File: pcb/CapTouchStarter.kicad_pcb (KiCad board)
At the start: 2 copper layers, 73.5 x 64 mm, 44 parts, among them J1 USB_C_Receptacle, J2 62684-50110, Q1 SS8050-G, Q2 SS8050-G, SW1 BOOT, SW2 EN, U1 1965-ESP32-WROOM-32E(8MB)CT-ND, U2 AMS1117-3.3, U3 CP2102N-A01-GQFN28

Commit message: Using 3V3 for display VCC.
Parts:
- C1, C3, C4, C5: value 0.1μF -> 0.1μF/50V
- R11: value 22.1KΩ -> 22K1Ω
- R14: value 47.5KΩ -> 47K5Ω
- R15: value 2K (5%) -> 2KΩ
- R17, R18: value 10K -> 10KΩ
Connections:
- J2 pad 1: VBUS -> +3V3
- R1 pad 2: VBUS -> +3V3
- R2 pad 2: VBUS -> +3V3
- R3 pad 2: VBUS -> +3V3
- R4 pad 2: VBUS -> +3V3
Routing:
- net VBUS: track 207.4 -> 90.4 mm, vias 2 -> 0
- net +3V3: track 246.8 -> 265.3 mm
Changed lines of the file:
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@@
     (thickness 1.6)
     (drawings 11)
-    (tracks 651)
+    (tracks 640)
     (zones 0)
     (modules 44)
@@
       (net 48 "Net-(J2-Pad2)"))
     (pad 1 smd rect (at -2 -11.65) (size 0.3 1.1) (layers F.Cu F.Paste F.Mask)
-      (net 15 VBUS))
+      (net 2 +3V3))
   )
   (module Capacitor_SMD:C_0603_1608Metric (layer F.Cu)
@@
       (effects (font (size 1 1) (thickness 0.15)))
     )
-    (fp_text value 0.1μF (at 5.588 -0.1905) (layer F.Fab)
+    (fp_text value 0.1μF/50V (at 5.588 -0.1905) (layer F.Fab)
       (effects (font (size 1 1) (thickness 0.15)))
     )
@@
       (effects (font (size 1 1) (thickness 0.15)))
     )
-    (fp_text value 0.1μF (at 0 1.43) (layer F.Fab)
+    (fp_text value 0.1μF/50V (at 0 1.43) (layer F.Fab)
       (effects (font (size 1 1) (thickness 0.15)))
     )
@@
       (effects (font (size 1 1) (thickness 0.15)))
     )
-    (fp_text value 0.1μF (at -1.283 2.9845 180) (layer F.Fab)
+    (fp_text value 0.1μF/50V (at -1.283 2.9845 180) (layer F.Fab)
       (effects (font (size 1 1) (thickness 0.15)))
     )
@@
       (effects (font (size 1 1) (thickness 0.15)))
     )
-    (fp_text value 0.1μF (at 0.127 -3.048 180) (layer F.Fab)
+    (fp_text value 0.1μF/50V (at 0.127 -3.048 180) (layer F.Fab)
       (effects (font (size 1 1) (thickness 0.15)))
     )
@@
     )
     (pad 2 smd roundrect (at 0.825 0 180) (size 0.8 0.95) (layers F.Cu F.Paste F.Mask) (roundrect_rratio 0.25)
-      (net 15 VBUS))
+      (net 2 +3V3))
     (pad 1 smd roundrect (at -0.825 0 180) (size 0.8 0.95) (layers F.Cu F.Paste F.Mask) (roundrect_rratio 0.25)
       (net 48 "Net-(J2-Pad2)"))
@@
       (net 47 "Net-(J2-Pad3)"))
     (pad 2 smd roundrect (at 0.825 0 180) (size 0.8 0.95) (layers F.Cu F.Paste F.Mask) (roundrect_rratio 0.25)
-      (net 15 VBUS))
+      (net 2 +3V3))
     (model ${KISYS3DMOD}/Resistor_SMD.3dshapes/R_0603_1608Metric.wrl
       (at (xyz 0 0 0))
@@
     )
     (pad 2 smd roundrect (at 0.825 0 180) (size 0.8 0.95) (layers F.Cu F.Paste F.Mask) (roundrect_rratio 0.25)
-      (net 15 VBUS))
+      (net 2 +3V3))
     (pad 1 smd roundrect (at -0.825 0 180) (size 0.8 0.95) (layers F.Cu F.Paste F.Mask) (roundrect_rratio 0.25)
       (net 46 "Net-(J2-Pad4)"))
@@
       (net 45 "Net-(J2-Pad5)"))
     (pad 2 smd roundrect (at 0.825 0 180) (size 0.8 0.95) (layers F.Cu F.Paste F.Mask) (roundrect_rratio 0.25)
-      (net 15 VBUS))
+      (net 2 +3V3))
     (model ${KISYS3DMOD}/Resistor_SMD.3dshapes/R_0603_1608Metric.wrl
       (at (xyz 0 0 0))
@@
       (effects (font (size 1 1) (thickness 0.15)))
     )
-    (fp_text value 22.1KΩ (at -0.635 2.794) (layer F.Fab)
+    (fp_text value 22K1Ω (at -0.635 2.794) (layer F.Fab)
       (effects (font (size 0.8 0.8) (thickness 0.1)))
     )
@@
       (effects (font (size 1 1) (thickness 0.15)))
     )
-    (fp_text value "2K (5%)" (at 0.127 3.6195 270) (layer F.Fab) hide
+    (fp_text value 2KΩ (at 0.127 3.6195 270) (layer F.Fab) hide
       (effects (font (size 0.5 0.5) (thickness 0.1)))
     )
@@
       (effects (font (size 1 1) (thickness 0.15)))
     )
-    (fp_text value 47.5KΩ (at 0.6985 2.794) (layer F.Fab)
+    (fp_text value 47K5Ω (at 0.6985 2.794) (layer F.Fab)
       (effects (font (size 0.8 0.8) (thickness 0.1)))
     )
@@
       (effects (font (size 1 1) (thickness 0.15)))
     )
-    (fp_text value 10K (at -0.1905 -2.8575 270) (layer F.Fab)
+    (fp_text value 10KΩ (at -0.1905 -2.8575 270) (layer F.Fab)
       (effects (font (size 1 1) (thickness 0.15)))
     )
@@
       (effects (font (size 1 1) (thickness 0.15)))
     )
-    (fp_text value 10K (at 0.0635 -2.921 270) (layer F.Fab)
+    (fp_text value 10KΩ (at 0.0635 -2.921 270) (layer F.Fab)
       (effects (font (size 1 1) (thickness 0.15)))
     )
@@
   (segment (start 175.768 85.9155) (end 174.244 84.3915) (width 0.6) (layer F.Cu) (net 2))
   (via (at 157.4165 84.3915) (size 0.8) (drill 0.4) (layers F.Cu B.Cu) (net 2))
-  (segment (start 174.244 84.3915) (end 157.4165 84.3915) (width 0.6) (layer F.Cu) (net 2))
   (via (at 191.77 89.535) (size 0.8) (drill 0.4) (layers F.Cu B.Cu) (net 2))
   (segment (start 175.768 85.9155) (end 179.197 85.9155) (width 0.4) (layer B.Cu) (net 2))
@@
   (segment (start 180.3395 124.4595) (end 182.9435 124.4595) (width 0.4) (layer F.Cu) (net 2))
   (segment (start 178.168 122.288) (end 180.3395 124.4595) (width 0.4) (layer F.Cu) (net 2))
+  (segment (start 168.593 92.075) (end 168.593 93.9165) (width 0.4) (layer F.Cu) (net 2))
+  (segment (start 168.593 93.9165) (end 168.593 95.758) (width 0.4) (layer F.Cu) (net 2))
+  (segment (start 168.593 95.758) (end 168.593 97.5995) (width 0.4) (layer F.Cu) (net 2))
+  (segment (start 172.2765 87.884) (end 172.2765 89.28) (width 0.25) (layer F.Cu) (net 2))
+  (segment (start 172.2765 89.28) (end 171.5135 90.043) (width 0.32) (layer F.Cu) (net 2))
+  (segment (start 168.593 90.106) (end 168.656 90.043) (width 0.4) (layer F.Cu) (net 2))
+  (segment (start 171.5135 90.043) (end 168.656 90.043) (width 0.4) (layer F.Cu) (net 2))
+  (segment (start 168.593 92.075) (end 168.593 90.106) (width 0.4) (layer F.Cu) (net 2))
+  (segment (start 168.656 84.4042) (end 168.6433 84.3915) (width 0.4) (layer F.Cu) (net 2))
+  (segment (start 168.656 90.043) (end 168.656 84.4042) (width 0.4) (layer F.Cu) (net 2))
+  (segment (start 168.6433 84.3915) (end 174.244 84.3915) (width 0.6) (layer F.Cu) (net 2))
+  (segment (start 157.4165 84.3915) (end 168.6433 84.3915) (width 0.6) (layer F.Cu) (net 2))
   (segment (start 134.252 80.137) (end 135.0645 80.137) (width 0.4) (layer F.Cu) (net 14))
   (segment (start 135.818 80.8905) (end 135.818 83.3525) (width 0.4) (layer F.Cu) (net 14))
@@
   (segment (start 160.0835 108.2835) (end 160.0835 106.045) (width 0.25) (layer F.Cu) (net 14))
   (segment (start 158.517499 104.478999) (end 159.7025 105.664) (width 0.25) (layer F.Cu) (net 14))
-  (segment (start 168.593 92.075) (end 168.593 93.9165) (width 0.4) (layer F.Cu) (net 15))
-  (segment (start 168.593 93.9165) (end 168.593 95.758) (width 0.4) (layer F.Cu) (net 15))
-  (segment (start 168.593 95.758) (end 168.593 97.5995) (width 0.4) (layer F.Cu) (net 15))
-  (segment (start 172.2765 87.884) (end 172.2765 89.28) (width 0.25) (layer F.Cu) (net 15))
-  (segment (start 172.2765 89.28) (end 171.5135 90.043) (width 0.32) (layer F.Cu) (net 15))
-  (segment (start 168.593 90.106) (end 168.656 90.043) (width 0.4) (layer F.Cu) (net 15))
-  (segment (start 168.656 90.043) (end 165.2905 90.043) (width 0.4) (layer F.Cu) (net 15))
-  (segment (start 168.593 92.075) (end 168.593 90.106) (width 0.4) (layer F.Cu) (net 15))
-  (segment (start 171.5135 90.043) (end 168.656 90.043) (width 0.4) (layer F.Cu) (net 15))
   (segment (start 133.4 137.909) (end 133.4135 137.9225) (width 0.25) (layer F.Cu) (net 15))
   (segment (start 133.4 134.9515) (end 133.4 137.909) (width 0.25) (layer F.Cu) (net 15))
@@
   (segment (start 169.2705 125.918) (end 169.0395 125.918) (width 0.4) (layer F.Cu) (net 15))
   (segment (start 167.16375 127.79375) (end 166.878 128.0795) (width 0.4) (layer F.Cu) (net 15))
-  (segment (start 169.0395 125.918) (end 167.16375 127.79375) (width 0.4) (layer F.Cu) (net 15))
   (segment (start 166.6875 128.524) (end 166.878 128.7145) (width 0.4) (layer F.Cu) (net 15))
   (segment (start 166.4335 128.524) (end 166.6875 128.524) (width 0.4) (layer F.Cu) (net 15))
@@
   (segment (start 131.192 134.9515) (end 131.064 134.8235) (width 0.4) (layer F.Cu) (net 15))
   (segment (start 133.4 134.9515) (end 131.192 134.9515) (width 0.4) (layer F.Cu) (net 15))
-  (segment (start 131.064 134.8235) (end 130.2515 134.8235) (width 0.6) (layer F.Cu) (net 15))
-  (segment (start 129.817999 134.389999) (end 129.817999 80.605499) (width 0.6) (layer F.Cu) (net 15))
-  (segment (start 130.2515 134.8235) (end 129.817999 134.389999) (width 0.6) (layer F.Cu) (net 15))
-  (segment (start 129.817999 80.605499) (end 131.619998 78.8035) (width 0.6) (layer F.Cu) (net 15))
-  (segment (start 131.619998 78.8035) (end 133.5405 78.8035) (width 0.6) (layer F.Cu) (net 15))
-  (segment (start 133.5405 78.8035) (end 159.639 78.8035) (width 0.6) (layer F.Cu) (net 15))
-  (via (at 160.655 79.8195) (size 0.8) (drill 0.4) (layers F.Cu B.Cu) (net 15))
-  (segment (start 159.639 78.8035) (end 160.655 79.8195) (width 0.6) (layer F.Cu) (net 15))
-  (via (at 160.655 86.4235) (size 0.8) (drill 0.4) (layers F.Cu B.Cu) (net 15))
-  (segment (start 160.655 79.8195) (end 160.655 86.4235) (width 0.6) (layer B.Cu) (net 15))
-  (segment (start 160.655 86.4235) (end 160.655 87.6935) (width 0.4) (layer F.Cu) (net 15))
-  (segment (start 163.0045 90.043) (end 165.2905 90.043) (width 0.4) (layer F.Cu) (net 15))
-  (segment (start 160.655 87.6935) (end 163.0045 90.043) (width 0.4) (layer F.Cu) (net 15))
   (segment (start 151.003 140.716) (end 151.0665 140.7795) (width 0.25) (layer F.Cu) (net 15))
   (segment (start 151.003 138.3665) (end 151.003 140.716) (width 0.25) (layer F.Cu) (net 15))
@@
   (segment (start 166.878 134.1755) (end 166.878 128.7145) (width 0.4) (layer F.Cu) (net 15))
   (segment (start 178.88 126.619) (end 178.88 127.0005) (width 0.4) (layer F.Cu) (net 15))
+  (segment (start 169.0395 125.918) (end 167.16375 127.79375) (width 0.4) (layer F.Cu) (net 15))
   (segment (start 138.754001 124.149501) (end 139.954 125.3495) (width 0.25) (layer F.Cu) (net 16))
   (segment (start 138.754001 121.478999) (end 138.754001 124.149501) (width 0.25) (layer F.Cu) (net 16))

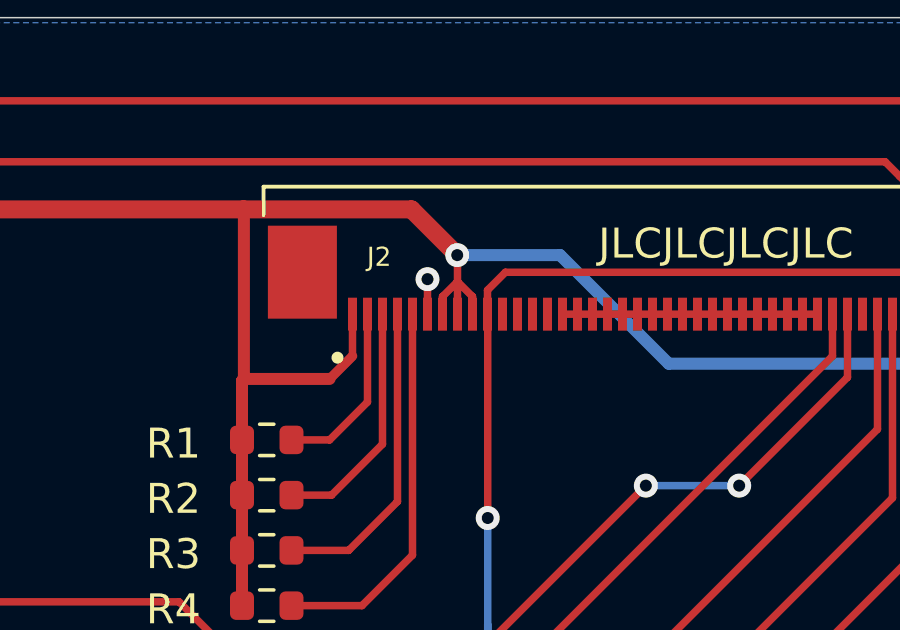
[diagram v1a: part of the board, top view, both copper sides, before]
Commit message: Switched display mode to 4-wires_8-bit SPI.
Set the interface mode pins (IM0..IM3) to [0, 1, 1, 0].
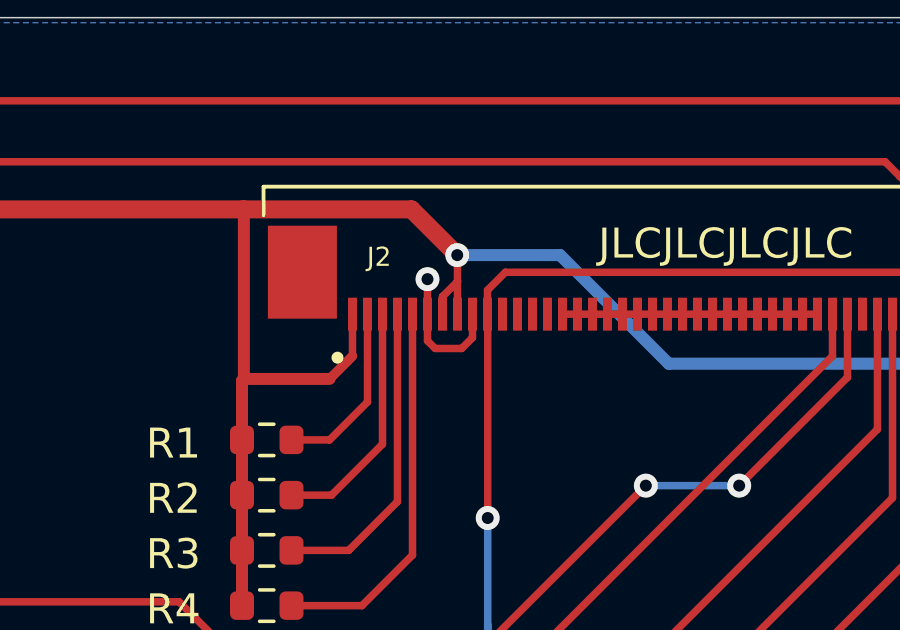
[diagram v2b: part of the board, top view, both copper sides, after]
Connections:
- J2 pad 9: +3V3 -> GND
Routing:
- net GND: track 77.7 -> 81.1 mm
- net +3V3: track 265.3 -> 264.1 mm

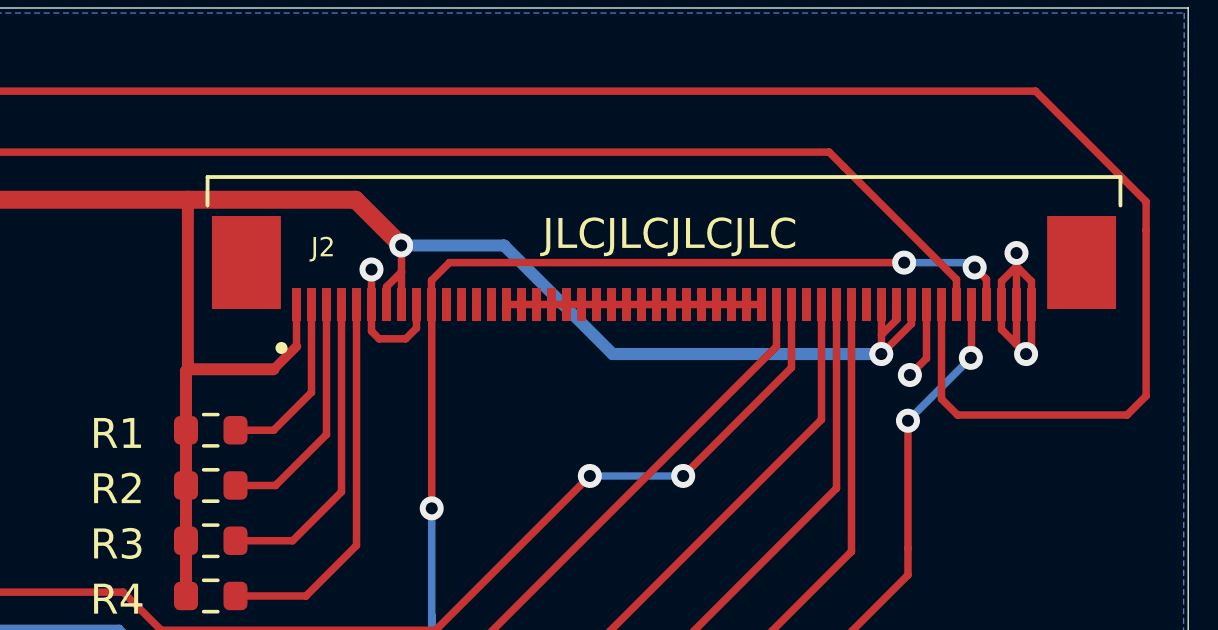
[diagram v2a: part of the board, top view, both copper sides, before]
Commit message: Connected display backlight cathode (LEDK) to GND.
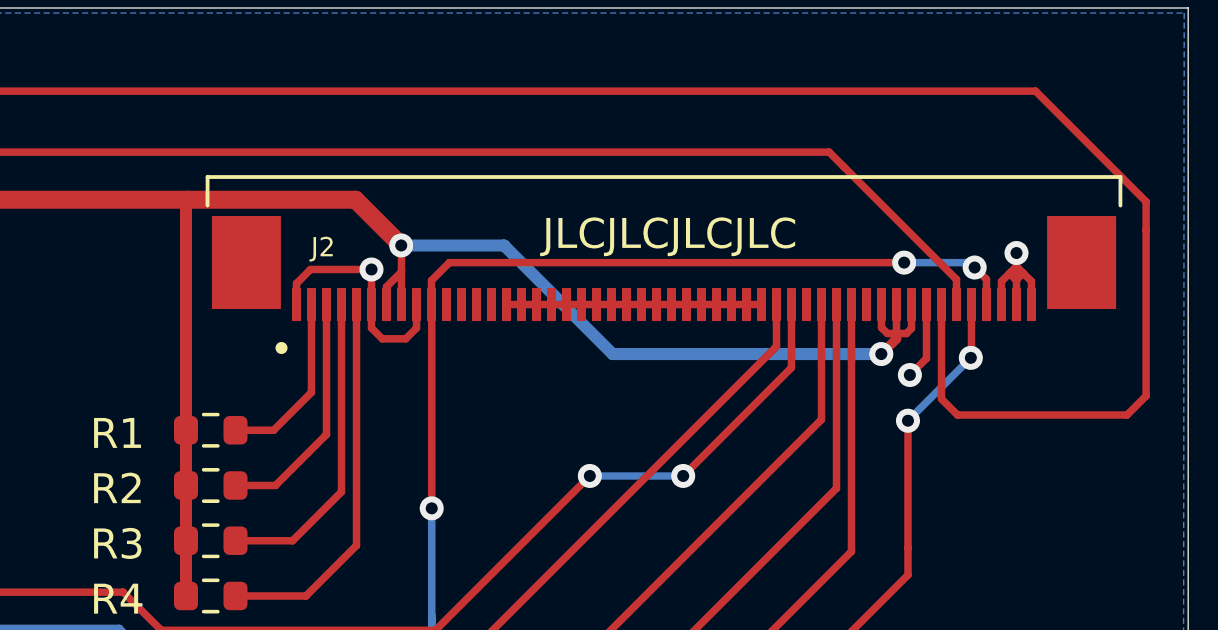
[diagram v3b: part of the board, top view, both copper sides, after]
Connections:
- J2 pad 1: +3V3 -> GND
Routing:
- net +3V3: track 264.1 -> 258.4 mm
- net GND: track 81.1 -> 80.1 mm, vias 43 -> 42

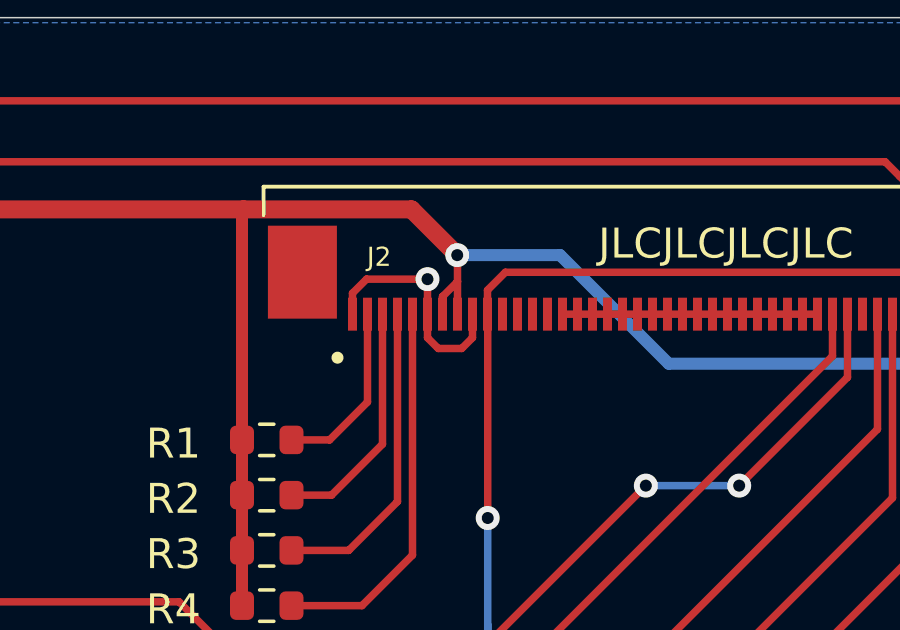
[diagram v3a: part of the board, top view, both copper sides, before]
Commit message: Back to 4-wire SPI II bus.
    Bus Sel
    [0,1,1,1]
    4-wires_8-bit SPI II
    /CS,RS,SDI,SDO,SCL
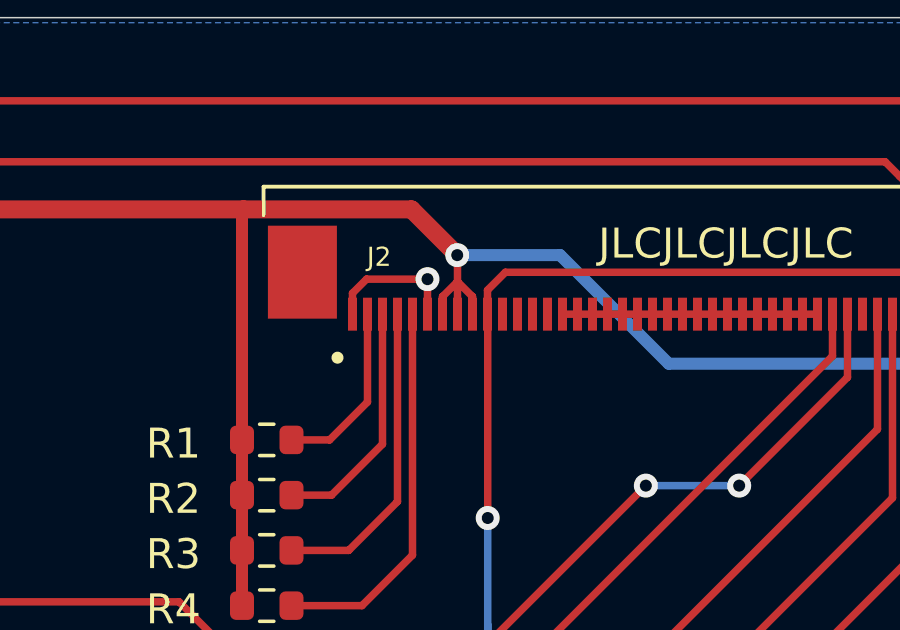
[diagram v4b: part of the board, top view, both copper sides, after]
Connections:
- J2 pad 9: GND -> +3V3
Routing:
- net GND: track 80.1 -> 76.7 mm
- net +3V3: track 258.4 -> 259.7 mm
